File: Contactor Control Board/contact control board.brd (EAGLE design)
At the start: 63.2 x 38.1 mm, 32 parts, among them Q4 MOSFET-NCHANNELFQP30N06L, U1 74ACT14SC

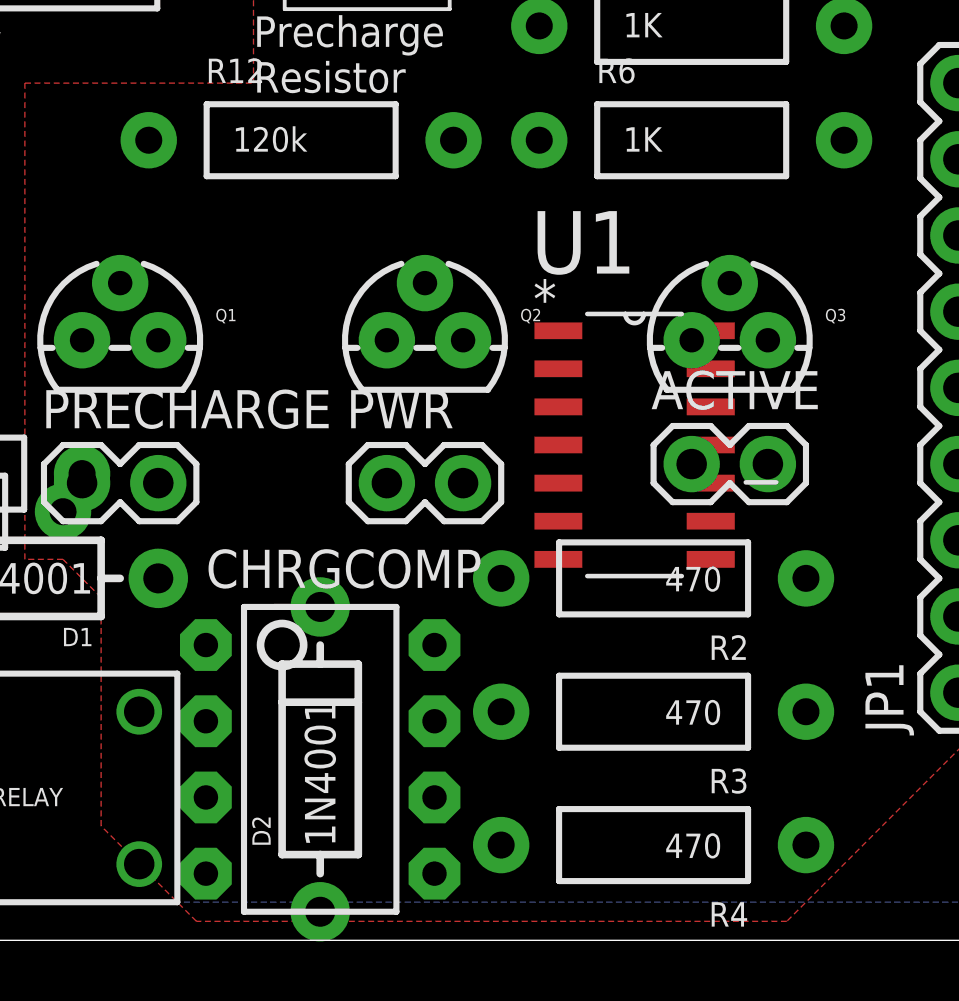
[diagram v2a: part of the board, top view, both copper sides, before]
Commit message: Replaced op-amp with voltage comparitor. Need to redo the voltage dividers for a 0-18V range or similar instead of 0-5V
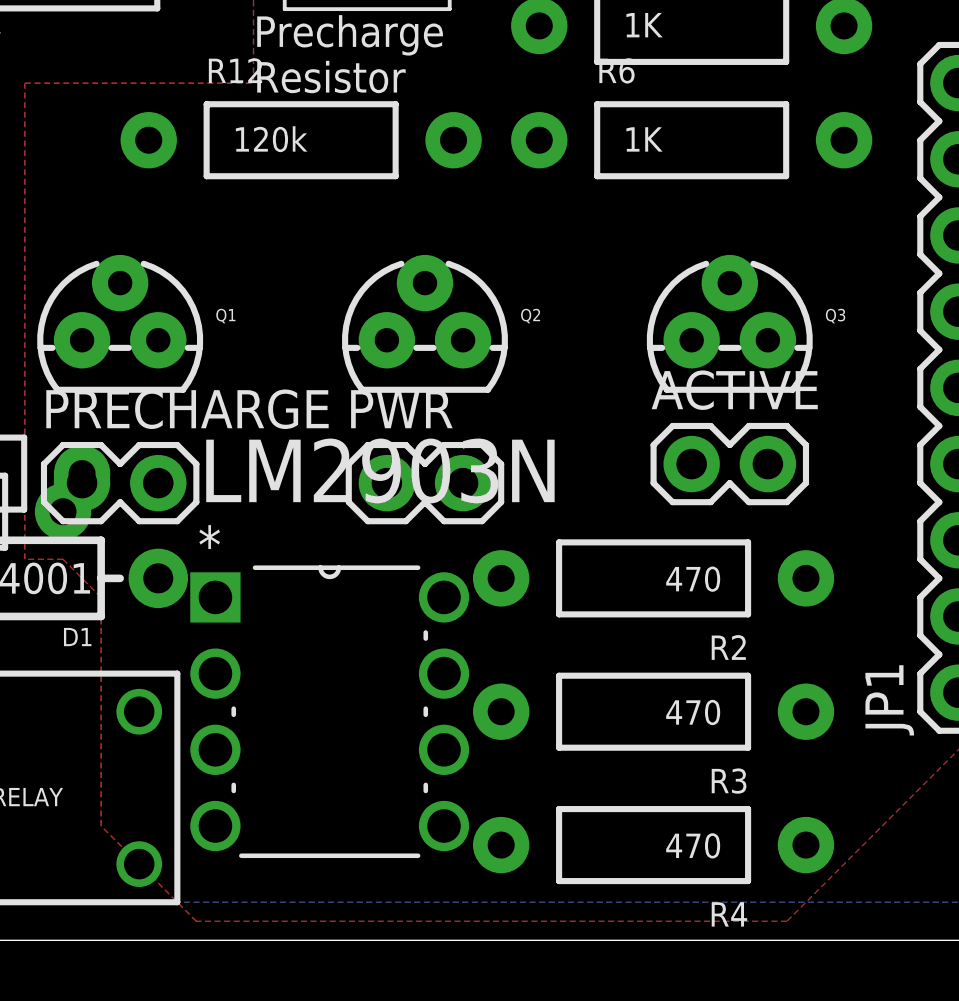
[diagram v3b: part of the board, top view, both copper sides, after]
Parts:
- removed CHRGCOMP: LM358, SparkFun-AnalogIC:DIP08
- removed D2: 1N4001, SparkFun-DiscreteSemi:DIODE-1N4001
- removed U1: 74ACT14SC, Fairchild_By_element14_Batch_1:SOIC127P600X175-14N
- added LM2903N: LM2903N, Fairchild_By_element14_Batch_1:DIP254P762X508-8
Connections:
- removed net N$5: CHRGCOMP.1, D2.A
- removed net N$6: U1.1
- net 5V: now also LM2903N.8; no longer CHRGCOMP.8, U1.14
- net CAP_CHARGE_REF: no longer CHRGCOMP.2
- net CAP_CHARGE_V_CURR: no longer CHRGCOMP.3
- net GND: now also LM2903N.4; no longer CHRGCOMP.4, U1.7
- net PRECH_STATE: now also LM2903N.1; no longer U1.2
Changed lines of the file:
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@@
 <setting verticaltext="up"/>
 </settings>
-<grid distance="0.0125" unitdist="inch" unit="inch" style="lines" multiple="1" display="yes" altdistance="0.005" altunitdist="inch" altunit="inch"/>
+<grid distance="0.05" unitdist="inch" unit="inch" style="lines" multiple="1" display="yes" altdistance="0.005" altunitdist="inch" altunit="inch"/>
 <layers>
 <layer number="1" name="Top" color="4" fill="1" visible="yes" active="yes"/>
@@
 <layer number="23" name="tOrigins" color="15" fill="1" visible="yes" active="yes"/>
 <layer number="24" name="bOrigins" color="15" fill="1" visible="yes" active="yes"/>
-<layer number="25" name="tNames" color="16" fill="1" visible="no" active="yes"/>
+<layer number="25" name="tNames" color="16" fill="1" visible="yes" active="yes"/>
 <layer number="26" name="bNames" color="16" fill="1" visible="no" active="yes"/>
 <layer number="27" name="tValues" color="7" fill="1" visible="no" active="yes"/>
@@
 <element name="RESISTOR" library="SparkFun-Connectors" package="1X02_2.54_SCREWTERM" value="M022.54MM_SCREWTERM" x="34.29" y="34.29"/>
 <element name="JP1" library="SparkFun-Connectors" package="1X09" value="M09" x="55.245" y="8.255" rot="R90"/>
-<element name="CHRGCOMP" library="SparkFun-AnalogIC" package="DIP08" value="LM358" x="33.9725" y="6.0325" rot="R270"/>
-<element name="D2" library="SparkFun-DiscreteSemi" package="DIODE-1N4001" value="1N4001" x="33.9725" y="6.0325" rot="R90"/>
 <element name="R8" library="SparkFun-Resistors" package="AXIAL-0.4" value="3M" x="16.51" y="5.08"/>
 <element name="R9" library="SparkFun-Resistors" package="AXIAL-0.4" value="120k" x="10.16" y="6.985"/>
@@
 <element name="R11" library="SparkFun-Resistors" package="AXIAL-0.4" value="120k" x="20.955" y="15.5575"/>
 <element name="R12" library="SparkFun-Resistors" package="AXIAL-0.4" value="120k" x="33.3375" y="26.67"/>
-<element name="U1" library="Fairchild_By_element14_Batch_1" package="SOIC127P600X175-14N" value="74ACT14SC" x="44.45" y="16.51">
-<attribute name="PACKAGE" value="SOIC-14" x="44.45" y="16.51" size="1.778" layer="27" font="vector" ratio="15" display="off"/>
-<attribute name="OC_NEWARK" value="78K6179" x="44.45" y="16.51" size="1.778" layer="27" font="vector" ratio="15" display="off"/>
-<attribute name="MPN" value="74ACT14SC" x="44.45" y="16.51" size="1.778" layer="27" font="vector" ratio="15" display="off"/>
-<attribute name="SUPPLIER" value="Fairchild" x="44.45" y="16.51" size="1.778" layer="27" font="vector" ratio="15" display="off"/>
-<attribute name="OC_FARNELL" value="3734936" x="44.45" y="16.51" size="1.778" layer="27" font="vector" ratio="15" display="off"/>
+<element name="LM2903N" library="Fairchild_By_element14_Batch_1" package="DIP254P762X508-8" value="LM2903N" x="38.1" y="3.81">
+<attribute name="PACKAGE" value="PDIP" x="38.1" y="3.81" size="1.778" layer="27" font="vector" ratio="15" display="off"/>
+<attribute name="OC_NEWARK" value="38C7339" x="38.1" y="3.81" size="1.778" layer="27" font="vector" ratio="15" display="off"/>
+<attribute name="MPN" value="LM2903N" x="38.1" y="3.81" size="1.778" layer="27" font="vector" ratio="15" display="off"/>
+<attribute name="SUPPLIER" value="FAIRCHILD SEMICONDUCTOR" x="38.1" y="3.81" size="1.778" layer="27" font="vector" ratio="15" display="off"/>
+<attribute name="OC_FARNELL" value="9487638" x="38.1" y="3.81" size="1.778" layer="27" font="vector" ratio="15" display="off"/>
 </element>
 </elements>
@@
 <contactref element="D1" pad="C"/>
 <contactref element="JP1" pad="2"/>
-<contactref element="CHRGCOMP" pad="8"/>
-<contactref element="U1" pad="14"/>
+<contactref element="LM2903N" pad="8"/>
 <wire x1="46.355" y1="15.875" x2="55.245" y2="10.795" width="0" layer="19" extent="1-1"/>
 <wire x1="36.195" y1="15.24" x2="46.355" y2="15.875" width="0" layer="19" extent="1-1"/>
-<wire x1="37.7825" y1="9.8425" x2="36.195" y2="15.24" width="0" layer="19" extent="1-1"/>
 <wire x1="26.035" y1="15.24" x2="36.195" y2="15.24" width="0" layer="19" extent="1-1"/>
 <wire x1="18.415" y1="12.065" x2="26.035" y2="15.24" width="0" layer="19" extent="1-1"/>
 <wire x1="20.32" y1="2.54" x2="18.415" y2="12.065" width="0" layer="19" extent="1-1"/>
-<wire x1="46.99" y1="20.32" x2="18.415" y2="12.065" width="0" layer="19" extent="1-1"/>
+<wire x1="38.1" y1="11.43" x2="18.415" y2="12.065" width="0" layer="19" extent="1-1"/>
 </signal>
 <signal name="GND">
@@
 <contactref element="Q3" pad="1"/>
 <contactref element="JP1" pad="1"/>
-<contactref element="CHRGCOMP" pad="4"/>
 <contactref element="OUTPUT" pad="5"/>
 <contactref element="R12" pad="P$2"/>
-<contactref element="U1" pad="7"/>
+<contactref element="LM2903N" pad="4"/>
 <wire x1="36.195" y1="20.0025" x2="46.355" y2="20.0025" width="0" layer="19" extent="1-1"/>
 <wire x1="38.4175" y1="26.67" x2="36.195" y2="20.0025" width="0" layer="19" extent="1-1"/>
@@
 <wire x1="8.255" y1="12.67" x2="14.605" y2="17.145" width="0" layer="19" extent="1-1"/>
 <wire x1="55.245" y1="8.255" x2="46.355" y2="20.0025" width="0" layer="19" extent="1-1"/>
-<wire x1="30.1625" y1="2.2225" x2="26.035" y2="20.0025" width="0" layer="19" extent="1-1"/>
-<wire x1="41.91" y1="12.7" x2="8.255" y2="12.67" width="0" layer="19" extent="1-1"/>
+<wire x1="30.48" y1="3.81" x2="8.255" y2="12.67" width="0" layer="19" extent="1-1"/>
 </signal>
 <signal name="CONTACT_EN">
@@
 <signal name="PRECH_STATE">
 <contactref element="JP1" pad="9"/>
-<contactref element="U1" pad="2"/>
-<wire x1="41.91" y1="19.05" x2="55.245" y2="28.575" width="0" layer="19" extent="1-1"/>
+<contactref element="LM2903N" pad="1"/>
+<wire x1="30.48" y1="11.43" x2="55.245" y2="28.575" width="0" layer="19" extent="1-1"/>
 </signal>
 <signal name="PRECHARGE_INPUT">
@@
 <wire x1="15.24" y1="6.985" x2="27.94" y2="2.54" width="0" layer="19" extent="1-1"/>
 </signal>
-<signal name="N$5">
-<contactref element="CHRGCOMP" pad="1"/>
-<contactref element="D2" pad="A"/>
-<wire x1="33.9725" y1="0.9525" x2="30.1625" y2="9.8425" width="0" layer="19" extent="1-1"/>
-</signal>
 <signal name="CAP_CHARGE_REF">
-<contactref element="CHRGCOMP" pad="2"/>
 <contactref element="R11" pad="P$2"/>
 <contactref element="R12" pad="P$1"/>
-<wire x1="30.1625" y1="7.3025" x2="26.035" y2="15.5575" width="0" layer="19" extent="1-1"/>
-<wire x1="28.2575" y1="26.67" x2="30.1625" y2="7.3025" width="0" layer="19" extent="1-1"/>
+<wire x1="26.035" y1="15.5575" x2="28.2575" y2="26.67" width="0" layer="19" extent="1-1"/>
 </signal>
 <signal name="N$3">
@@
 <contactref element="R8" pad="P$2"/>
 <contactref element="R9" pad="P$1"/>
-<contactref element="CHRGCOMP" pad="3"/>
-<wire x1="21.59" y1="5.08" x2="30.1625" y2="4.7625" width="0" layer="19" extent="1-1"/>
 <wire x1="5.08" y1="6.985" x2="21.59" y2="5.08" width="0" layer="19" extent="1-1"/>
 </signal>
-<signal name="N$6">
-<contactref element="U1" pad="1"/>
-</signal>
 </signals>

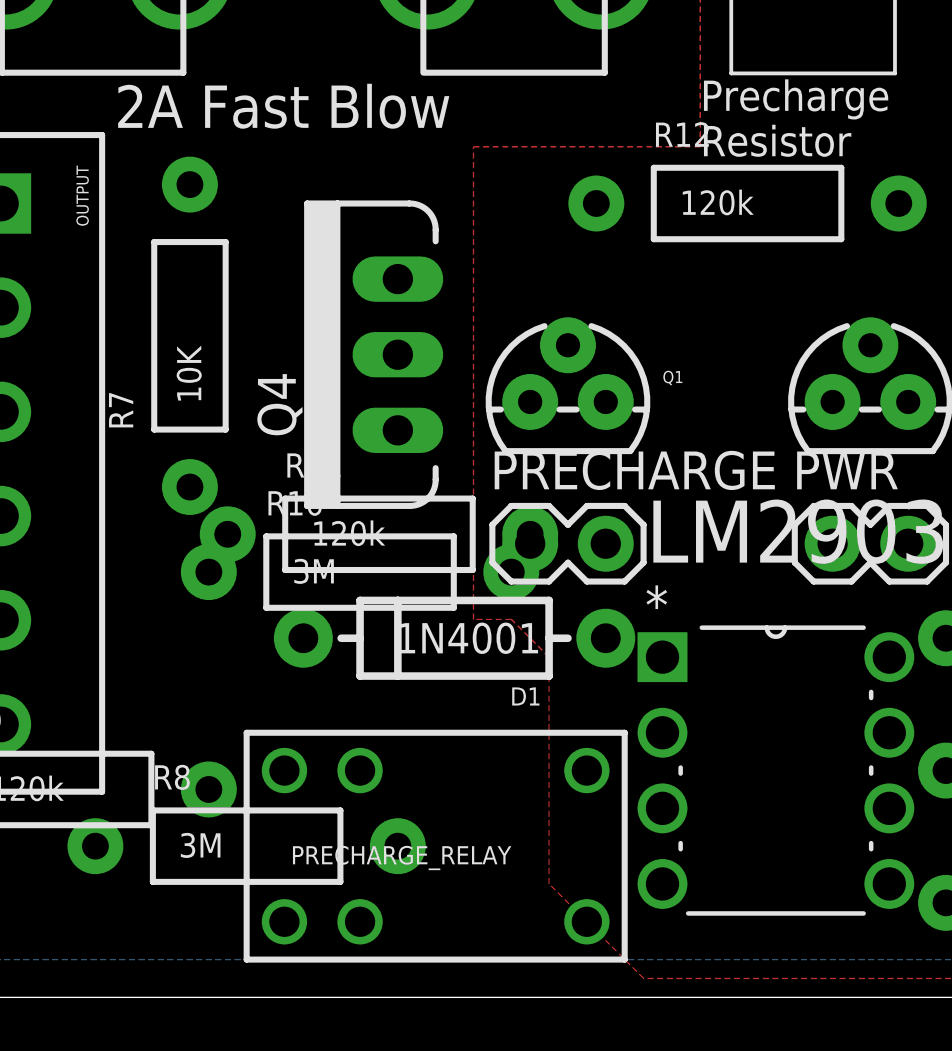
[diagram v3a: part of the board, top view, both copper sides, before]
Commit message: Updating voltage dividers to common resistor values
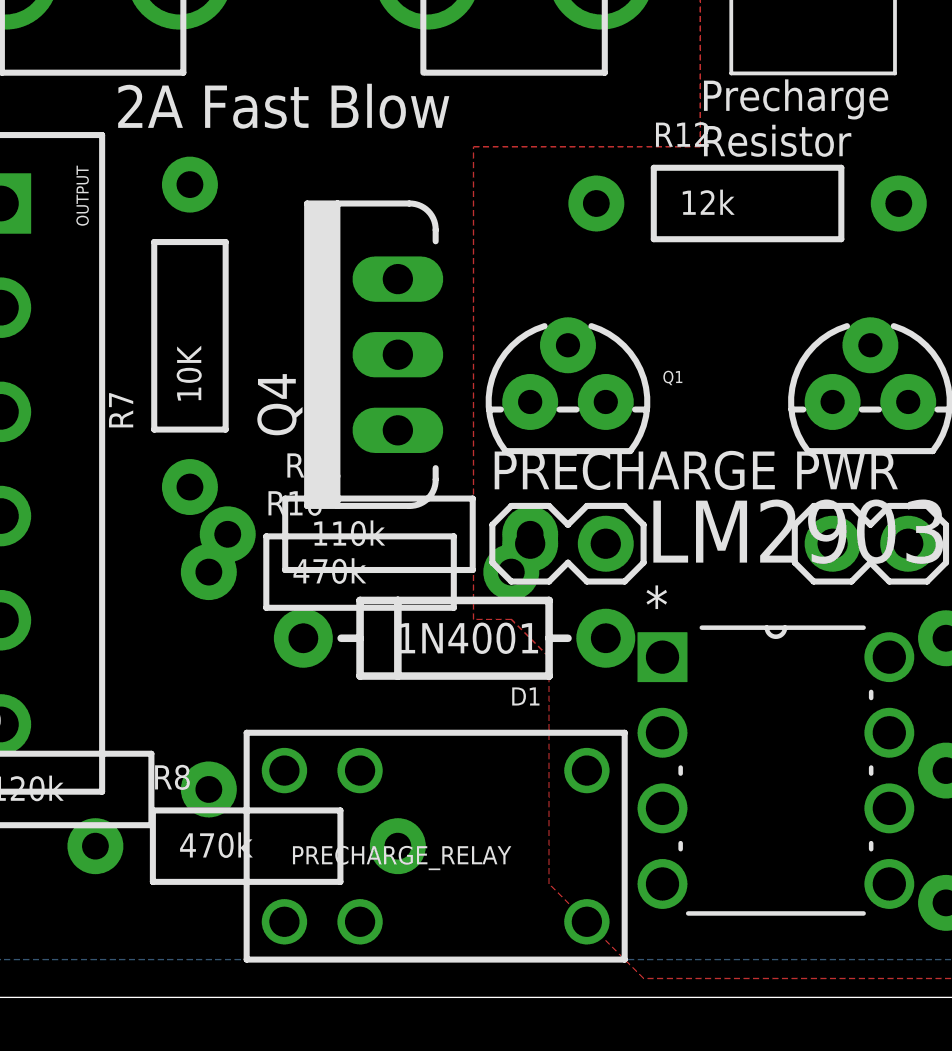
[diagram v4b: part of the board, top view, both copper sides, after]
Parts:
- R10, R8: value 3M -> 470k
- R11: value 120k -> 110k
- R12: value 120k -> 12k
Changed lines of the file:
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@@
 <layer number="23" name="tOrigins" color="15" fill="1" visible="yes" active="yes"/>
 <layer number="24" name="bOrigins" color="15" fill="1" visible="yes" active="yes"/>
-<layer number="25" name="tNames" color="16" fill="1" visible="yes" active="yes"/>
+<layer number="25" name="tNames" color="16" fill="1" visible="no" active="yes"/>
 <layer number="26" name="bNames" color="16" fill="1" visible="no" active="yes"/>
 <layer number="27" name="tValues" color="7" fill="1" visible="no" active="yes"/>
@@
 <element name="RESISTOR" library="SparkFun-Connectors" package="1X02_2.54_SCREWTERM" value="M022.54MM_SCREWTERM" x="34.29" y="34.29"/>
 <element name="JP1" library="SparkFun-Connectors" package="1X09" value="M09" x="55.245" y="8.255" rot="R90"/>
-<element name="R8" library="SparkFun-Resistors" package="AXIAL-0.4" value="3M" x="16.51" y="5.08"/>
+<element name="R8" library="SparkFun-Resistors" package="AXIAL-0.4" value="470k" x="16.51" y="5.08"/>
 <element name="R9" library="SparkFun-Resistors" package="AXIAL-0.4" value="120k" x="10.16" y="6.985"/>
-<element name="R10" library="SparkFun-Resistors" package="AXIAL-0.4" value="3M" x="20.32" y="14.2875"/>
-<element name="R11" library="SparkFun-Resistors" package="AXIAL-0.4" value="120k" x="20.955" y="15.5575"/>
-<element name="R12" library="SparkFun-Resistors" package="AXIAL-0.4" value="120k" x="33.3375" y="26.67"/>
+<element name="R10" library="SparkFun-Resistors" package="AXIAL-0.4" value="470k" x="20.32" y="14.2875"/>
+<element name="R11" library="SparkFun-Resistors" package="AXIAL-0.4" value="110k" x="20.955" y="15.5575"/>
+<element name="R12" library="SparkFun-Resistors" package="AXIAL-0.4" value="12k" x="33.3375" y="26.67"/>
 <element name="LM2903N" library="Fairchild_By_element14_Batch_1" package="DIP254P762X508-8" value="LM2903N" x="38.1" y="3.81">
 <attribute name="PACKAGE" value="PDIP" x="38.1" y="3.81" size="1.778" layer="27" font="vector" ratio="15" display="off"/>
